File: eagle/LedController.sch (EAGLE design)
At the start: 32 parts, among them IC1 MCP601R, Q1 16MHz, Q5 PMV20EN, X1 2510-, X2 MKDSN1,5/4-5,08

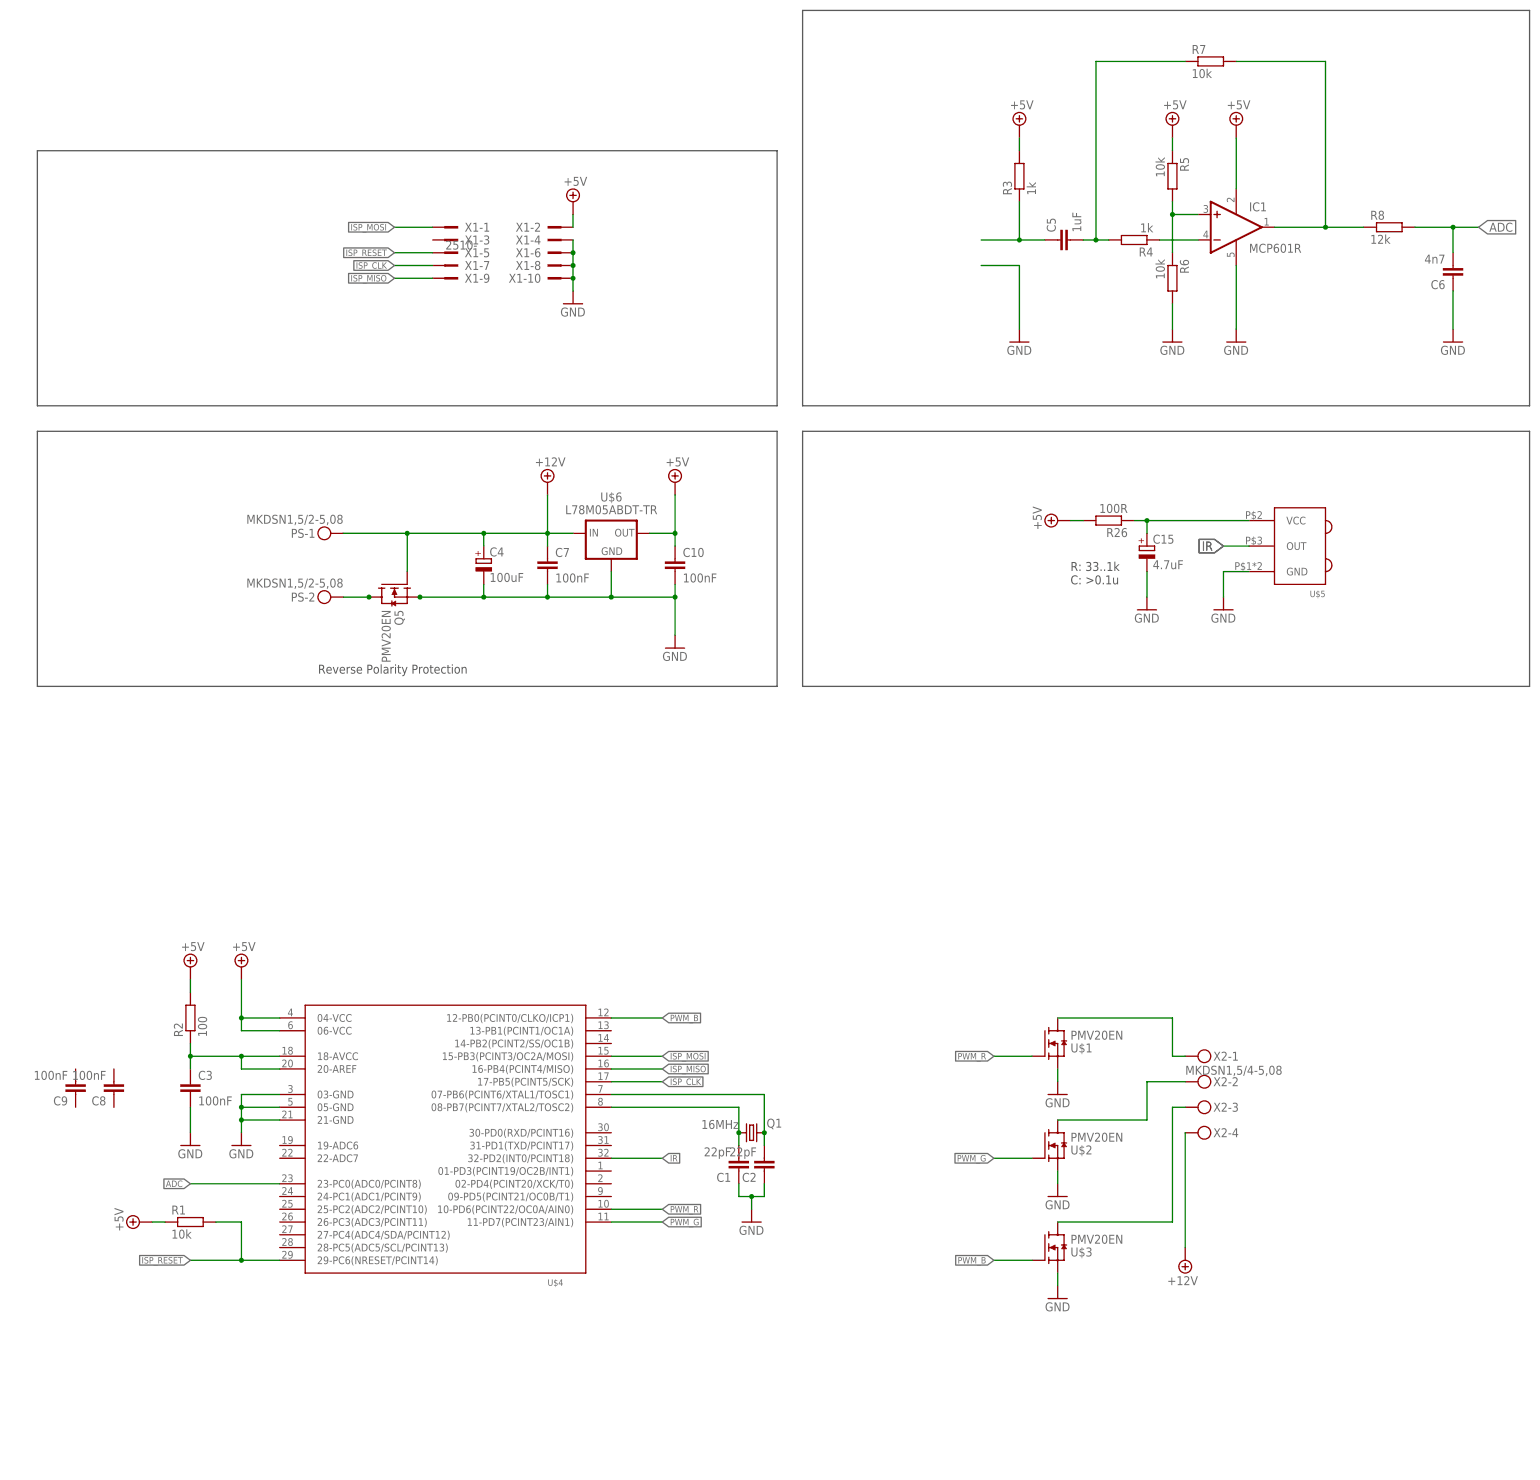
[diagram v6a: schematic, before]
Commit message: Add DC Barrel Jack
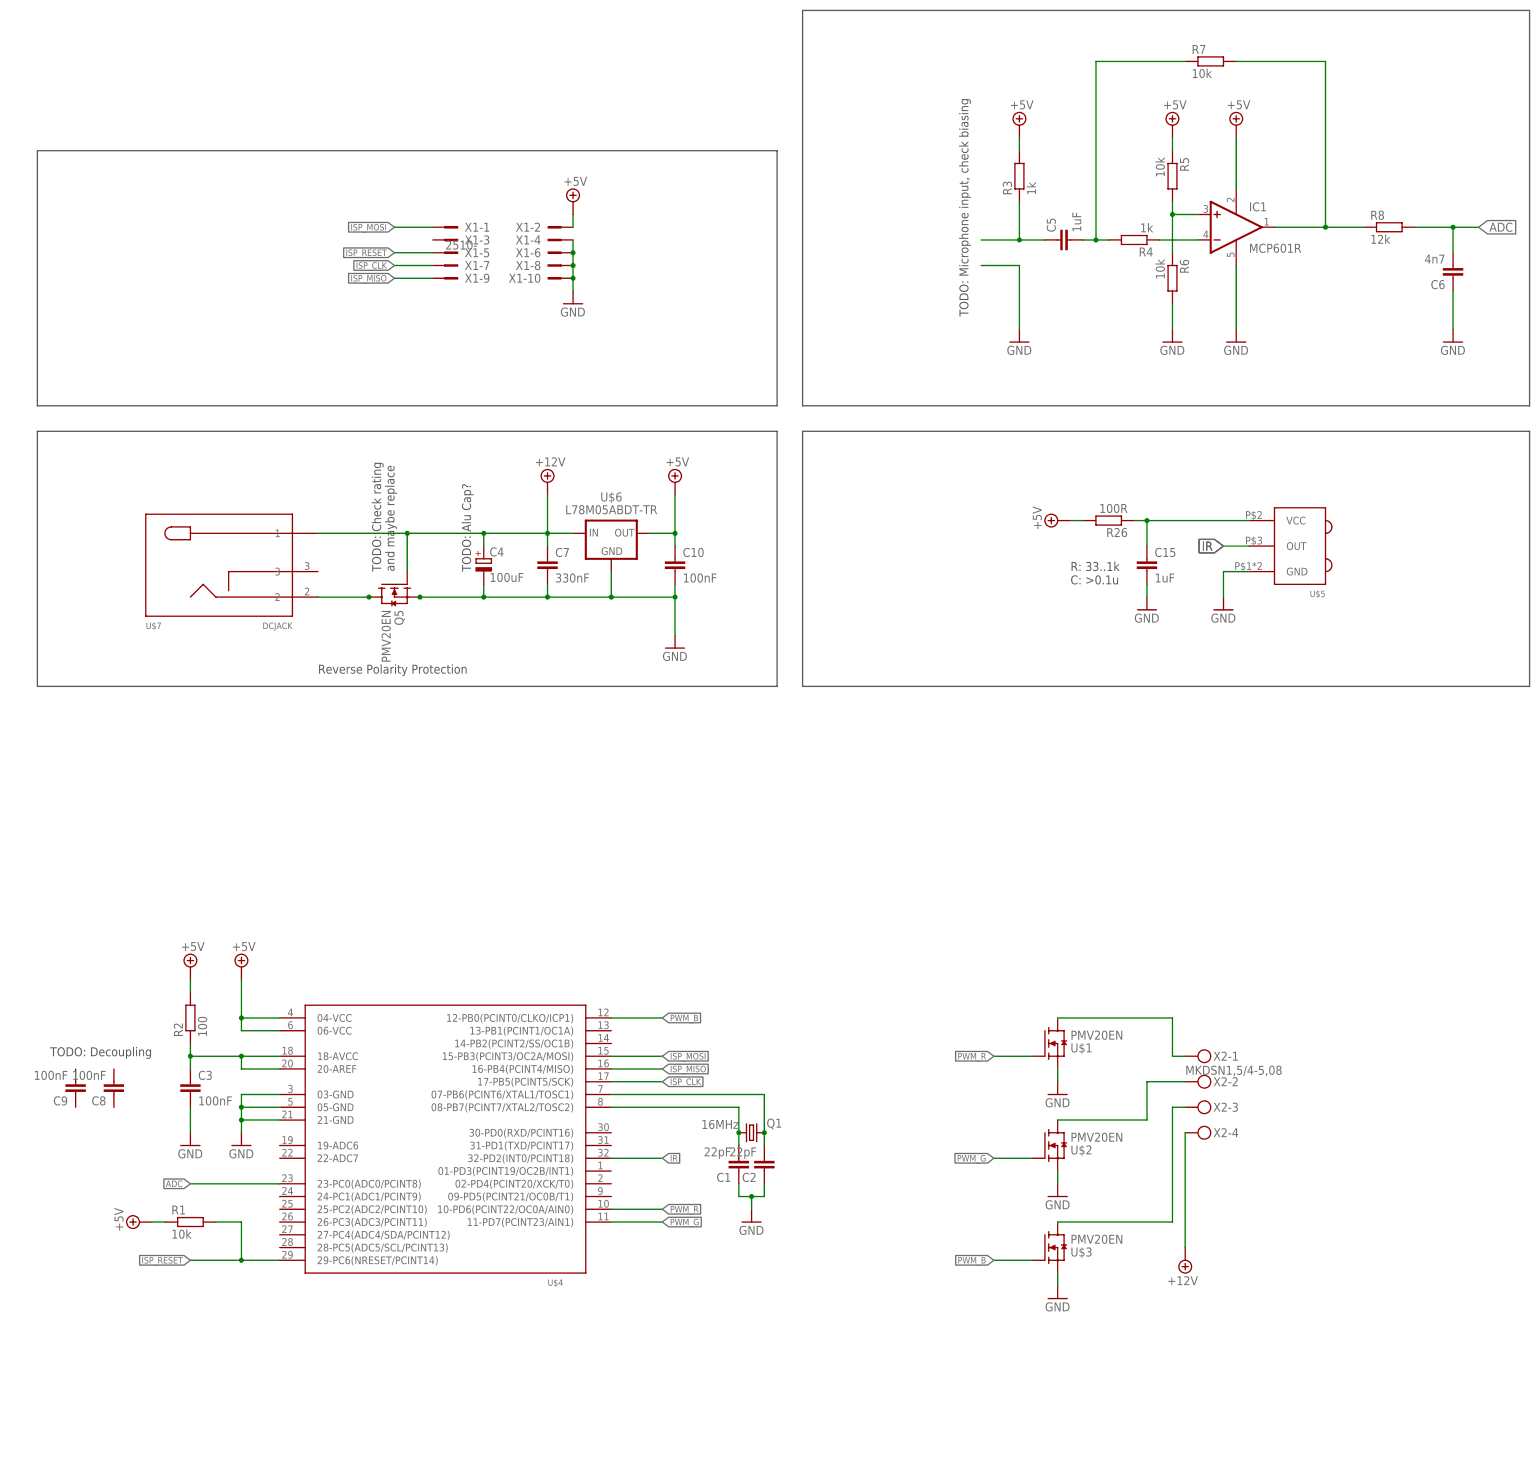
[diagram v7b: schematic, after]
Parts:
- removed PS: MKDSN1,5/2-5,08, con-phoenix-508:MKDSN1,5/2-5,08
- added U$7: DCJACK, LedController:DCJACK
- C15: value 4.7uF -> 1uF; device rcl:CPOL-EUE2-5 -> rcl:C-EUC0805
- C4: device rcl:CPOL-EUE2-5 -> rcl:CPOL-EU153CLV-0605
- C7: value 100nF -> 330nF
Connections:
- net +12V: now also U$7.1; no longer PS-1.KL
- net GND: now also C15.2; no longer C15.-
- net N$63: now also C15.1; no longer C15.+
- net N$8: now also U$7.2; no longer PS-2.KL
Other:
- note added: "TODO: Alu Cap?"
- note added: "TODO: Check rating and maybe replace"
- note added: "TODO: Decoupling"
- note added: "TODO: Microphone input, check biasing"
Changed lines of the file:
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@@
 <part name="GND4" library="supply1" deviceset="GND" device=""/>
 <part name="GND8" library="supply1" deviceset="GND" device=""/>
-<part name="C7" library="rcl" deviceset="C-EU" device="C0805" value="100nF"/>
+<part name="C7" library="rcl" deviceset="C-EU" device="C0805" value="330nF"/>
 <part name="C9" library="rcl" deviceset="C-EU" device="C0805" value="100nF"/>
 <part name="GND16" library="supply1" deviceset="GND" device=""/>
 <part name="R26" library="rcl" deviceset="R-EU_" device="R0805" value="100R"/>
 <part name="C10" library="rcl" deviceset="C-EU" device="C0805" value="100nF"/>
-<part name="C15" library="rcl" deviceset="CPOL-EU" device="E2-5" value="4.7uF"/>
+<part name="C15" library="rcl" deviceset="C-EU" device="C0805" value="1uF"/>
 <part name="X1" library="con-3m" deviceset="2510-" device=""/>
-<part name="C4" library="rcl" deviceset="CPOL-EU" device="E2-5" value="100uF"/>
+<part name="C4" library="rcl" deviceset="CPOL-EU" device="153CLV-0605" value="100uF"/>
 <part name="GND2" library="supply1" deviceset="GND" device=""/>
 <part name="GND6" library="supply1" deviceset="GND" device=""/>
 <part name="GND9" library="supply1" deviceset="GND" device=""/>
-<part name="PS" library="con-phoenix-508" deviceset="MKDSN1,5/2-5,08" device=""/>
 <part name="GND5" library="supply1" deviceset="GND" device=""/>
 <part name="GND7" library="supply1" deviceset="GND" device=""/>
@@
 <part name="U$5" library="LedController" deviceset="TSOP75236" device=""/>
 <part name="U$6" library="LedController" deviceset="L78M05ABDT-TR" device=""/>
+<part name="U$7" library="LedController" deviceset="DCJACK" device=""/>
 </parts>
 <sheets>
@@
 <text x="208.28" y="175.26" size="1.778" layer="97">R: 33..1k
 C: &gt;0.1u</text>
+<text x="73.66" y="177.8" size="1.778" layer="97" rot="R90">TODO: Check rating
+and maybe replace</text>
+<text x="5.08" y="81.28" size="1.778" layer="97">TODO: Decoupling</text>
+<text x="187.96" y="228.6" size="1.778" layer="97" rot="R90">TODO: Microphone input, check biasing</text>
+<text x="88.9" y="177.8" size="1.778" layer="97" rot="R90">TODO: Alu Cap?</text>
 </plain>
 <instances>
@@
 <instance part="R26" gate="G$1" x="215.9" y="187.96" rot="R180"/>
 <instance part="C10" gate="G$1" x="129.54" y="180.34"/>
-<instance part="C15" gate="G$1" x="223.52" y="182.88"/>
+<instance part="C15" gate="G$1" x="223.52" y="180.34"/>
 <instance part="X1" gate="-1" x="86.36" y="246.38" rot="R180"/>
 <instance part="X1" gate="-2" x="104.14" y="246.38"/>
@@
 <instance part="GND6" gate="1" x="205.74" y="73.66"/>
 <instance part="GND9" gate="1" x="144.78" y="48.26"/>
-<instance part="PS" gate="-1" x="60.96" y="185.42" rot="R180"/>
-<instance part="PS" gate="-2" x="60.96" y="172.72" rot="R180"/>
 <instance part="GND5" gate="1" x="205.74" y="53.34"/>
 <instance part="GND7" gate="1" x="205.74" y="33.02"/>
@@
 <instance part="U$5" gate="G$1" x="254" y="182.88" rot="MR0"/>
 <instance part="U$6" gate="G$1" x="116.84" y="185.42"/>
+<instance part="U$7" gate="G$1" x="40.64" y="177.8"/>
 </instances>
 <busses>
@@
 <segment>
 <pinref part="GND16" gate="1" pin="GND"/>
-<pinref part="C15" gate="G$1" pin="-"/>
-<wire x1="223.52" y1="177.8" x2="223.52" y2="172.72" width="0.1524" layer="91"/>
+<pinref part="C15" gate="G$1" pin="2"/>
+<wire x1="223.52" y1="175.26" x2="223.52" y2="172.72" width="0.1524" layer="91"/>
 </segment>
 <segment>
@@
 <segment>
 <pinref part="R26" gate="G$1" pin="1"/>
-<pinref part="C15" gate="G$1" pin="+"/>
-<wire x1="223.52" y1="185.42" x2="223.52" y2="187.96" width="0.1524" layer="91"/>
+<pinref part="C15" gate="G$1" pin="1"/>
+<wire x1="223.52" y1="182.88" x2="223.52" y2="187.96" width="0.1524" layer="91"/>
 <pinref part="U$5" gate="G$1" pin="VCC"/>
 <wire x1="223.52" y1="187.96" x2="220.98" y2="187.96" width="0.1524" layer="91"/>
@@
 </segment>
 <segment>
-<pinref part="PS" gate="-1" pin="KL"/>
-<wire x1="63.5" y1="185.42" x2="76.2" y2="185.42" width="0.1524" layer="91"/>
 <pinref part="Q5" gate="PMV20EN$1" pin="G"/>
 <wire x1="76.2" y1="177.8" x2="76.2" y2="185.42" width="0.1524" layer="91"/>
@@
 <wire x1="104.14" y1="185.42" x2="104.14" y2="193.04" width="0.1524" layer="91"/>
 <pinref part="U$6" gate="G$1" pin="IN"/>
+<pinref part="U$7" gate="G$1" pin="1"/>
+<wire x1="58.42" y1="185.42" x2="76.2" y2="185.42" width="0.1524" layer="91"/>
 </segment>
 </net>
@@
 <net name="N$8" class="0">
 <segment>
-<pinref part="PS" gate="-2" pin="KL"/>
 <pinref part="Q5" gate="PMV20EN$1" pin="D"/>
-<wire x1="63.5" y1="172.72" x2="68.58" y2="172.72" width="0.1524" layer="91"/>
 <pinref part="Q5" gate="PMV20EN$1" pin="D"/>
 <junction x="68.58" y="172.72"/>
 <pinref part="Q5" gate="PMV20EN$1" pin="D"/>
 <pinref part="Q5" gate="PMV20EN$1" pin="D"/>
-</segment>
-</net>
+<pinref part="U$7" gate="G$1" pin="2"/>
+<wire x1="68.58" y1="172.72" x2="58.42" y2="172.72" width="0.1524" layer="91"/>
+</segment>
+</net>

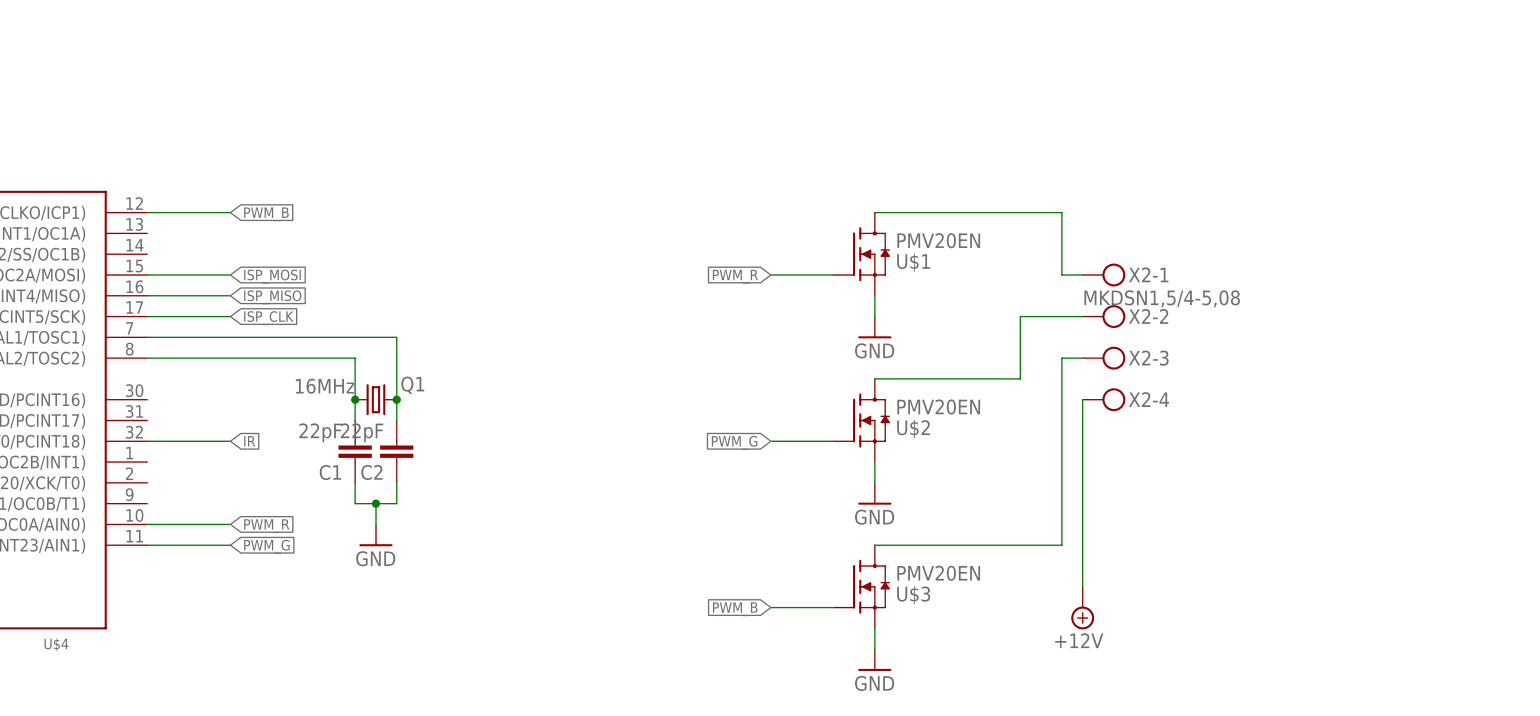
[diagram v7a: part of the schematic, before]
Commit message: Cosmetic Changes in Board Schematic
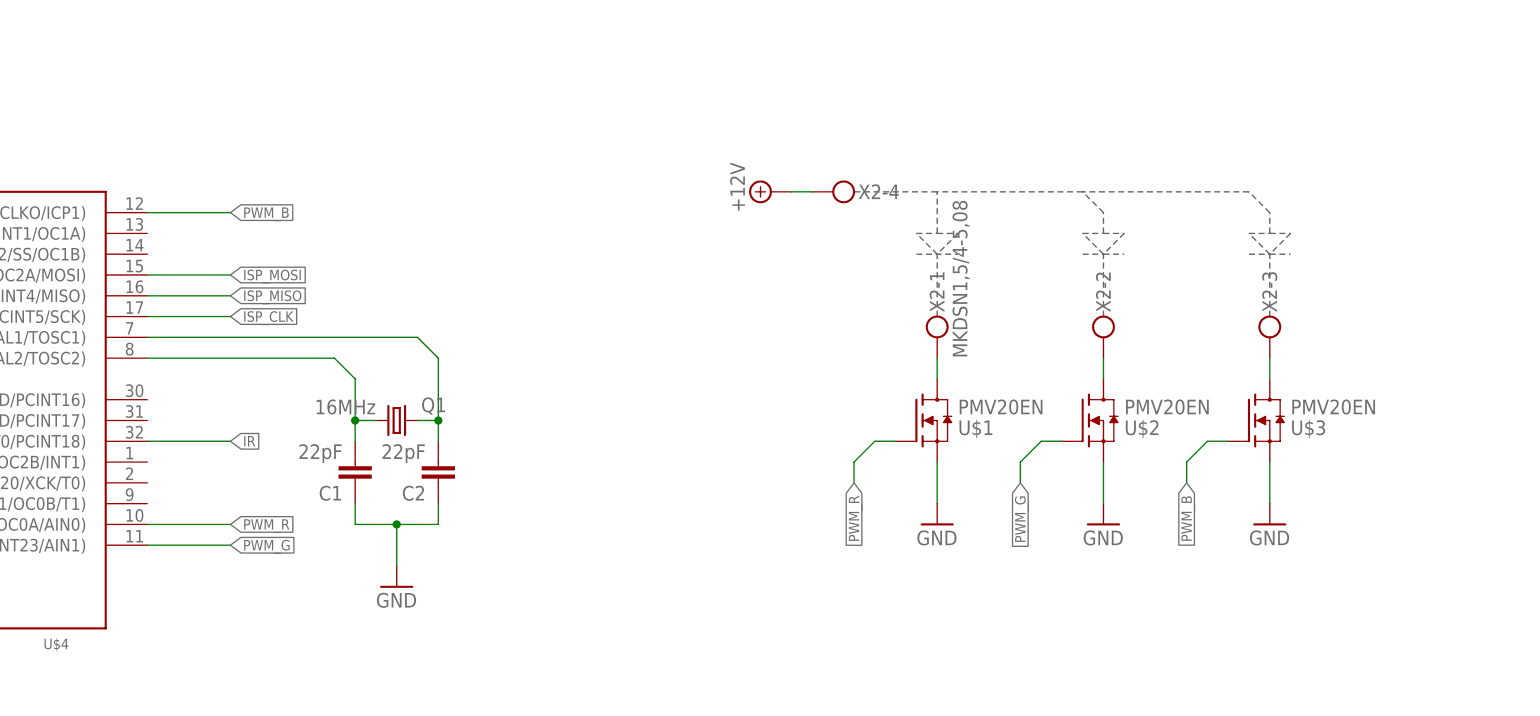
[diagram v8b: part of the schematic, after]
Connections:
- new net N$2: C1.2, Q1.2
- net N$13: no longer C1.2, Q1.2
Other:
- moved on the sheet: C1, C2, Q1, U$1, U$2, U$3, X2-1, X2-2, X2-3, X2-4
